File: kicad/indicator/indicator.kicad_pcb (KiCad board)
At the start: 2 copper layers, 44.7 x 13.7 mm, 9 parts, among them J1 Conn_01x03, Q1 2N3904, Q2 2N3904

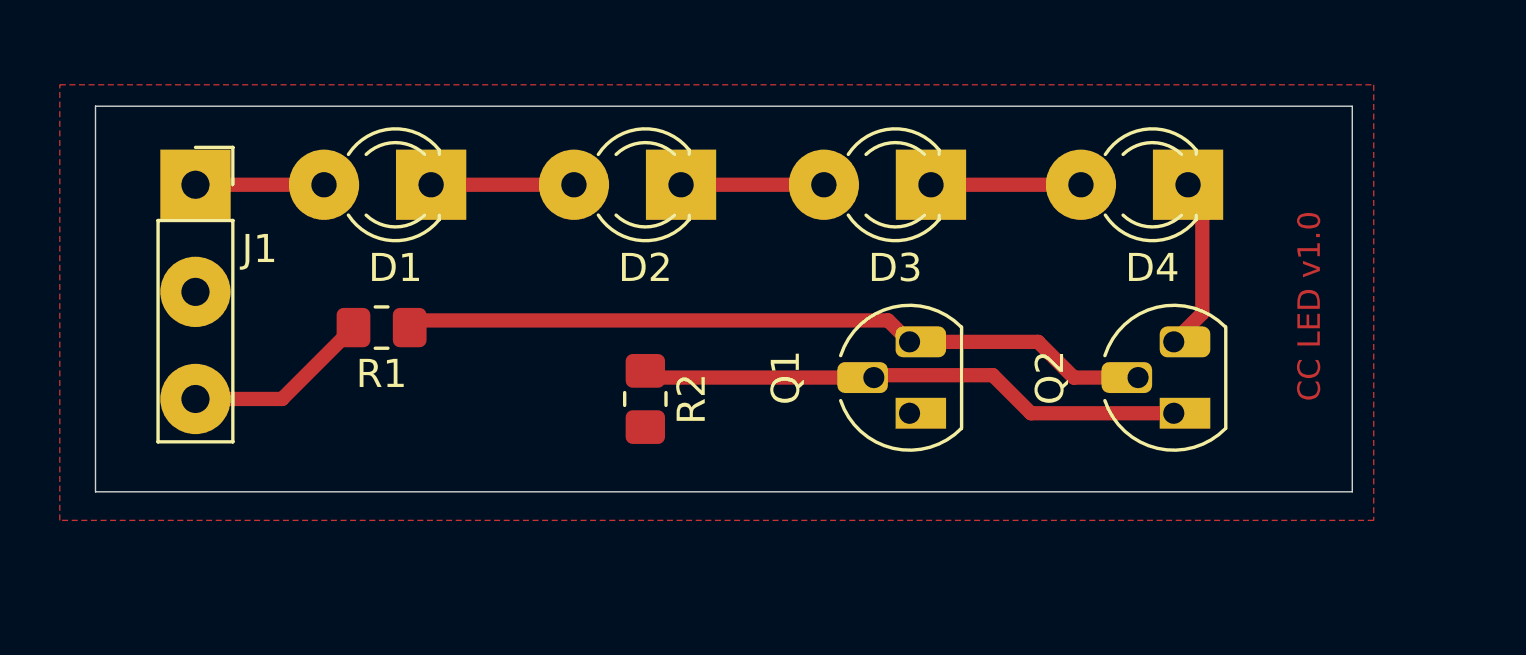
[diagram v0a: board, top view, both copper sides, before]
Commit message: add footprint for bjts
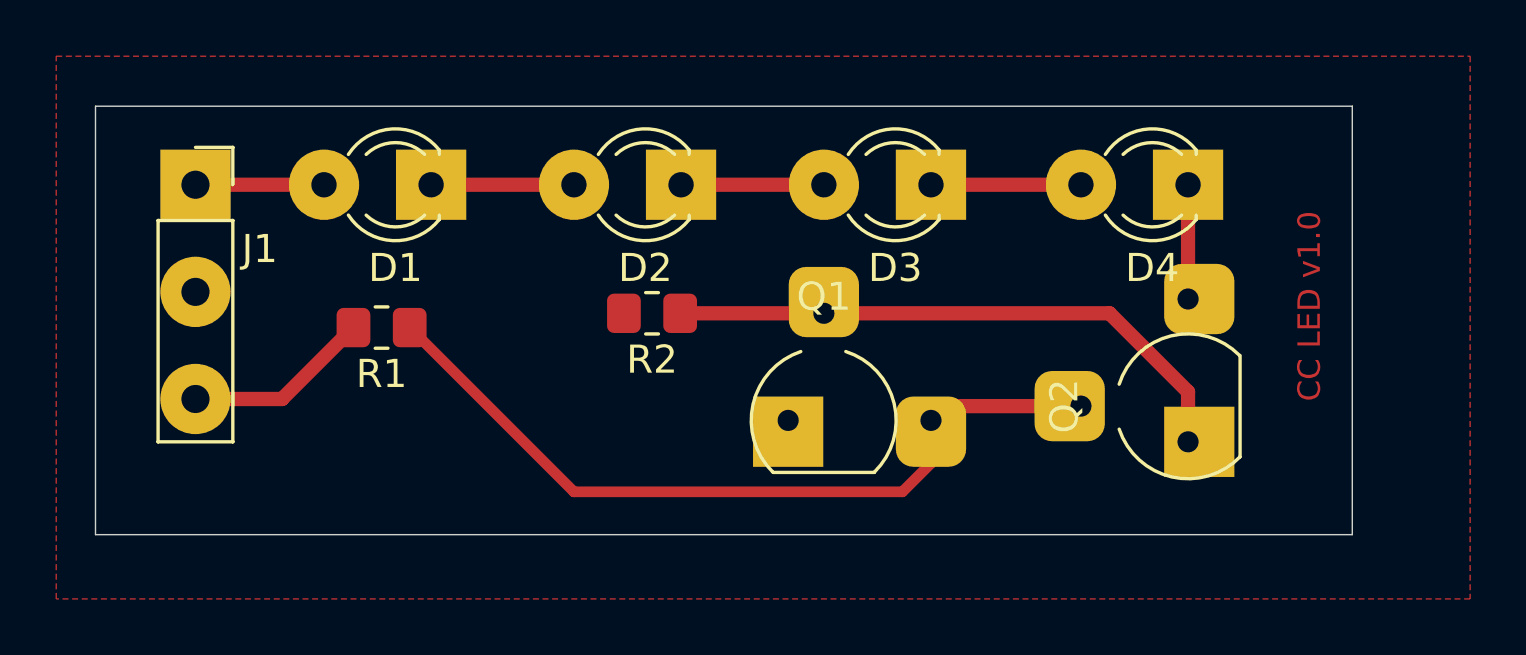
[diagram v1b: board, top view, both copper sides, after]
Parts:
- Q1, Q2: footprint Package_TO_SOT_THT:TO-92_HandSolder -> indicator:TO-92_HandSolder_Large_Pad
- moved Q1 4.33 mm to (39.6, 26.9), turned to 0 degrees
- moved R2 3.06 mm to (34.8, 23.1), turned to 180 degrees
- moved Q2 1.14 mm to (53.8, 27.7)
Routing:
- net Net-(Q1-Pad3): track 26.9 -> 28.8 mm
- net Net-(D4-Pad1): track 6.01 -> 4.06 mm
- net Net-(Q1-Pad2): track 19.5 -> 21.3 mm
- net Net-(D2-Pad1): track 5.59 -> 5.08 mm
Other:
- board size 44.7 x 13.7 mm -> 44.7 x 15.2 mm

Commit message: Add resistors values
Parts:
- R1: value R -> 5.1k
- R2: value R -> 39
